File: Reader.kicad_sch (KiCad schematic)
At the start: 41 parts, among them J1 Conn_01x04, J2 Amphenol Dubox ‎76383-402LF‎, J3 Conn_01x04, J4 Conn_01x08, J5 Conn_01x10, J6 Conn_01x03, J7 Conn_01x02, Q1 2N7002, Q2 2N7002, Q3 2N7002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

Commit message: Enlarge mounting holes
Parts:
- H1, H2, H3: footprint MountingHole:MountingHole_2.5mm -> MountingHole:MountingHole_3.2mm_M3
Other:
- note added: "TODO: - Mark LED + on silk - Cut groundplane below cutout to prevent making loop/antenna. - Resistor values on silk? - 2N7002 hand soldering footprint - Reduce thermal size (esp C1 and transistors). Maybe just remove traces, or also -0,05mm? - decoupling/buffer caps? - Use only 1 GND of NFC reader(for EMI)? - Remove 45deg silkscreen line at J1 Done: - Removed optional from pulldowns, made value 1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"
- note removed: "TODO: - Mark LED + on silk - Cut groundplane below cutout to prevent making loop/antenna. - Resistor values on silk? - 2N7002 hand soldering footprint - Reduce thermal size (esp C1 and transistors). Maybe just remove traces, or also -0,05mm? - decoupling/buffer caps? - Use only 1 GND of NFC reader(for EMI)? - Remove 45deg silkscreen line at J1 - Larger holes 3.2mm Done: - Removed optional from pu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"
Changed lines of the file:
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@@
     (stroke (width 0) (type default))
   )
-  (text "TODO:\n - Mark LED + on silk\n - Cut groundplane below cutout to prevent making loop/antenna.\n - Resistor values on silk?\n - 2N7002 hand soldering footprint\n - Reduce thermal size (esp C1 and transistors). Maybe just remove traces, or also -0,05mm?\n - decoupling/buffer caps?\n - Use only 1 GND of NFC reader(for EMI)?\n - Remove 45deg silkscreen line at J1\n - Larger holes 3.2mm\n\nDone:\n - Removed optional from pulldowns, made value 1k.\n - Added series resistors for button input\n - Added C2 to suppress output pin pulses"
+  (text "TODO:\n - Mark LED + on silk\n - Cut groundplane below cutout to prevent making loop/antenna.\n - Resistor values on silk?\n - 2N7002 hand soldering footprint\n - Reduce thermal size (esp C1 and transistors). Maybe just remove traces, or also -0,05mm?\n - decoupling/buffer caps?\n - Use only 1 GND of NFC reader(for EMI)?\n - Remove 45deg silkscreen line at J1\n\nDone:\n - Removed optional from pulldowns, made value 1k.\n - Added series resistors for button input\n - Added C2 to suppress output pin pulses\n - Enlarged mounting holes from 2.5mm to 3.2mm\n"
     (at 116.84 152.4 0)
     (effects (font (size 1.27 1.27)) (justify left bottom))
@@
       (effects (font (size 1.27 1.27)) (justify left))
     )
-    (property "Footprint" "MountingHole:MountingHole_2.5mm" (at 265.43 147.32 0)
+    (property "Footprint" "MountingHole:MountingHole_3.2mm_M3" (at 265.43 147.32 0)
       (effects (font (size 1.27 1.27)) hide)
     )
@@
       (effects (font (size 1.27 1.27)) (justify left))
     )
-    (property "Footprint" "MountingHole:MountingHole_2.5mm" (at 265.43 153.67 0)
+    (property "Footprint" "MountingHole:MountingHole_3.2mm_M3" (at 265.43 153.67 0)
       (effects (font (size 1.27 1.27)) hide)
     )
@@
       (effects (font (size 1.27 1.27)) (justify left))
     )
-    (property "Footprint" "MountingHole:MountingHole_2.5mm" (at 265.43 160.02 0)
-      (effects (font (size 1.27 1.27)) hide)
-    )
+    (property "Footprint" "MountingHole:MountingHole_3.2mm_M3" (at 265.43 160.02 0)
+      (effects (font (size 1.27 1.27)) hide)
+    )

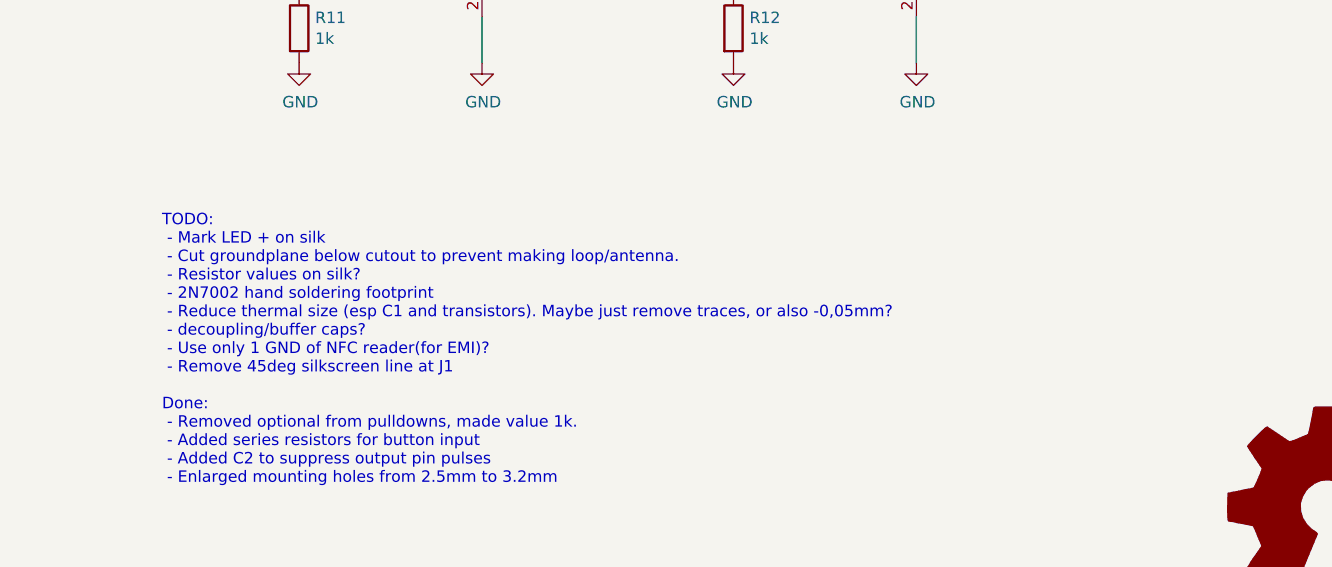
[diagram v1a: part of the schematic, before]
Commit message: Remove groundloop-related todos
It seems that having multiple GND connections and a hole inside the GND
plane might not actually be problematic (or if it is, making a horseshoe
out of it might not make it better).

So for now, leave this as is until it is actually a problem.
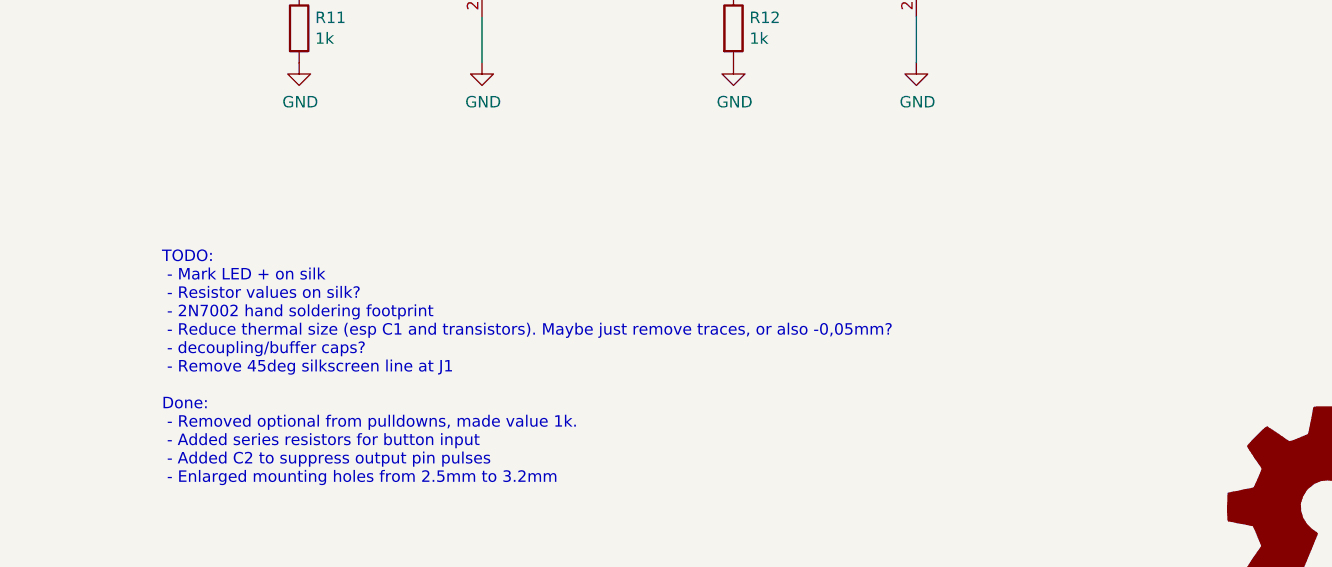
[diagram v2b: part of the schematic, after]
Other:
- note added: "TODO: - Mark LED + on silk - Resistor values on silk? - 2N7002 hand soldering footprint - Reduce thermal size (esp C1 and transistors). Maybe just remove traces, or also -0,05mm? - decoupling/buffer caps? - Remove 45deg silkscreen line at J1 Done: - Removed optional from pulldowns, made value 1k. - Added series resistors for button input - Added C2 to suppress output pin pulses - Enlarged mountin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"
- note removed: "TODO: - Mark LED + on silk - Cut groundplane below cutout to prevent making loop/antenna. - Resistor values on silk? - 2N7002 hand soldering footprint - Reduce thermal size (esp C1 and transistors). Maybe just remove traces, or also -0,05mm? - decoupling/buffer caps? - Use only 1 GND of NFC reader(for EMI)? - Remove 45deg silkscreen line at J1 Done: - Removed optional from pulldowns, made value 1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"
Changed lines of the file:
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@@
     (stroke (width 0) (type default))
   )
-  (text "TODO:\n - Mark LED + on silk\n - Cut groundplane below cutout to prevent making loop/antenna.\n - Resistor values on silk?\n - 2N7002 hand soldering footprint\n - Reduce thermal size (esp C1 and transistors). Maybe just remove traces, or also -0,05mm?\n - decoupling/buffer caps?\n - Use only 1 GND of NFC reader(for EMI)?\n - Remove 45deg silkscreen line at J1\n\nDone:\n - Removed optional from pulldowns, made value 1k.\n - Added series resistors for button input\n - Added C2 to suppress output pin pulses\n - Enlarged mounting holes from 2.5mm to 3.2mm\n"
+  (text "TODO:\n - Mark LED + on silk\n - Resistor values on silk?\n - 2N7002 hand soldering footprint\n - Reduce thermal size (esp C1 and transistors). Maybe just remove traces, or also -0,05mm?\n - decoupling/buffer caps?\n - Remove 45deg silkscreen line at J1\n\nDone:\n - Removed optional from pulldowns, made value 1k.\n - Added series resistors for button input\n - Added C2 to suppress output pin pulses\n - Enlarged mounting holes from 2.5mm to 3.2mm\n"
     (at 116.84 152.4 0)
     (effects (font (size 1.27 1.27)) (justify left bottom))

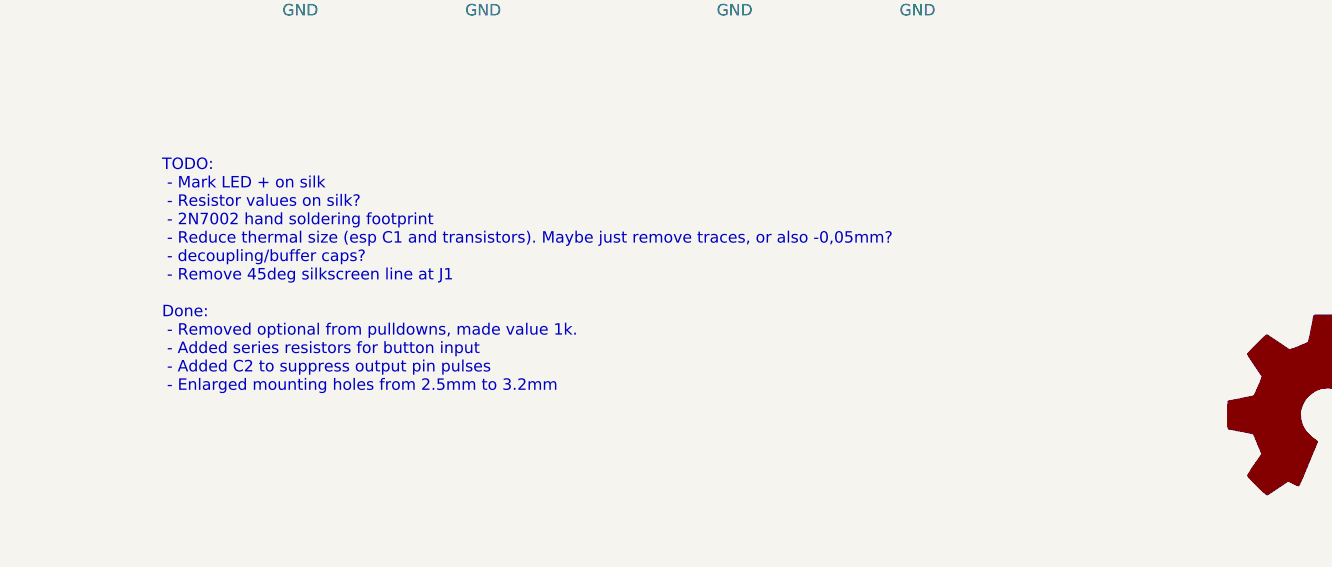
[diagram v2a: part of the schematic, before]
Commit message: Mark LED polarity on silkscreen
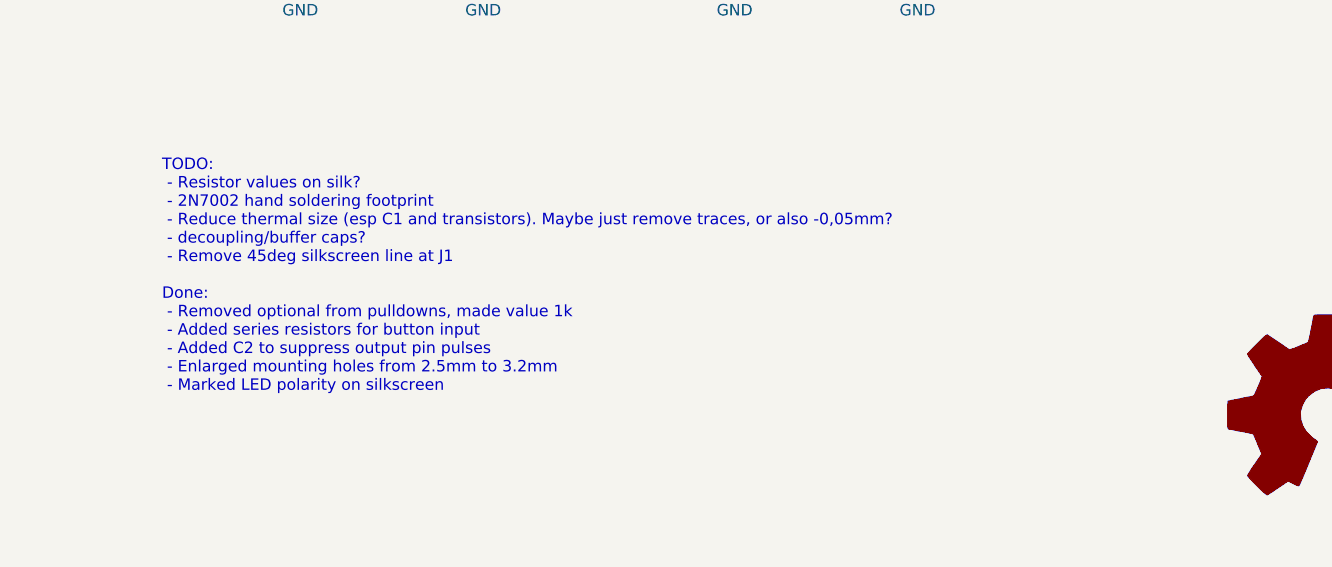
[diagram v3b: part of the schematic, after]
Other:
- note added: "TODO: - Resistor values on silk? - 2N7002 hand soldering footprint - Reduce thermal size (esp C1 and transistors). Maybe just remove traces, or also -0,05mm? - decoupling/buffer caps? - Remove 45deg silkscreen line at J1 Done: - Removed optional from pulldowns, made value 1k - Added series resistors for button input - Added C2 to suppress output pin pulses - Enlarged mounting holes from 2.5mm to 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"
- note removed: "TODO: - Mark LED + on silk - Resistor values on silk? - 2N7002 hand soldering footprint - Reduce thermal size (esp C1 and transistors). Maybe just remove traces, or also -0,05mm? - decoupling/buffer caps? - Remove 45deg silkscreen line at J1 Done: - Removed optional from pulldowns, made value 1k. - Added series resistors for button input - Added C2 to suppress output pin pulses - Enlarged mountin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"
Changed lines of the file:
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@@
     (stroke (width 0) (type default))
   )
-  (text "TODO:\n - Mark LED + on silk\n - Resistor values on silk?\n - 2N7002 hand soldering footprint\n - Reduce thermal size (esp C1 and transistors). Maybe just remove traces, or also -0,05mm?\n - decoupling/buffer caps?\n - Remove 45deg silkscreen line at J1\n\nDone:\n - Removed optional from pulldowns, made value 1k.\n - Added series resistors for button input\n - Added C2 to suppress output pin pulses\n - Enlarged mounting holes from 2.5mm to 3.2mm\n"
+  (text "TODO:\n - Resistor values on silk?\n - 2N7002 hand soldering footprint\n - Reduce thermal size (esp C1 and transistors). Maybe just remove traces, or also -0,05mm?\n - decoupling/buffer caps?\n - Remove 45deg silkscreen line at J1\n\nDone:\n - Removed optional from pulldowns, made value 1k\n - Added series resistors for button input\n - Added C2 to suppress output pin pulses\n - Enlarged mounting holes from 2.5mm to 3.2mm\n - Marked LED polarity on silkscreen\n"
     (at 116.84 152.4 0)
     (effects (font (size 1.27 1.27)) (justify left bottom))

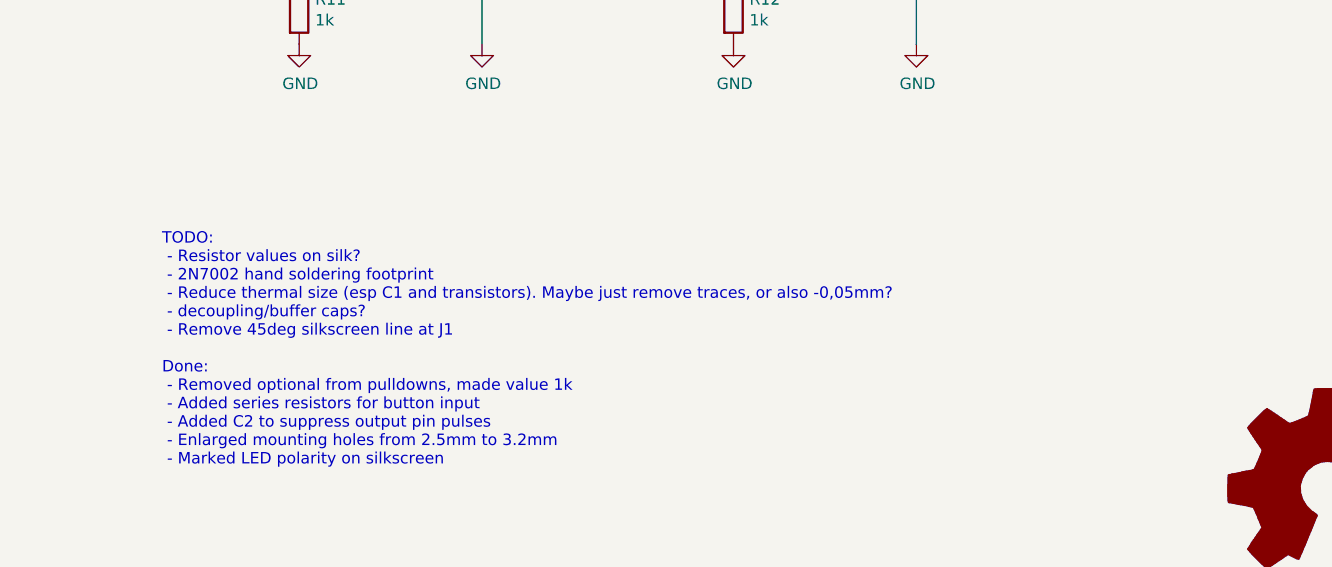
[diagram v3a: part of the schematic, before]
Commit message: Remove unintended silkscreen line
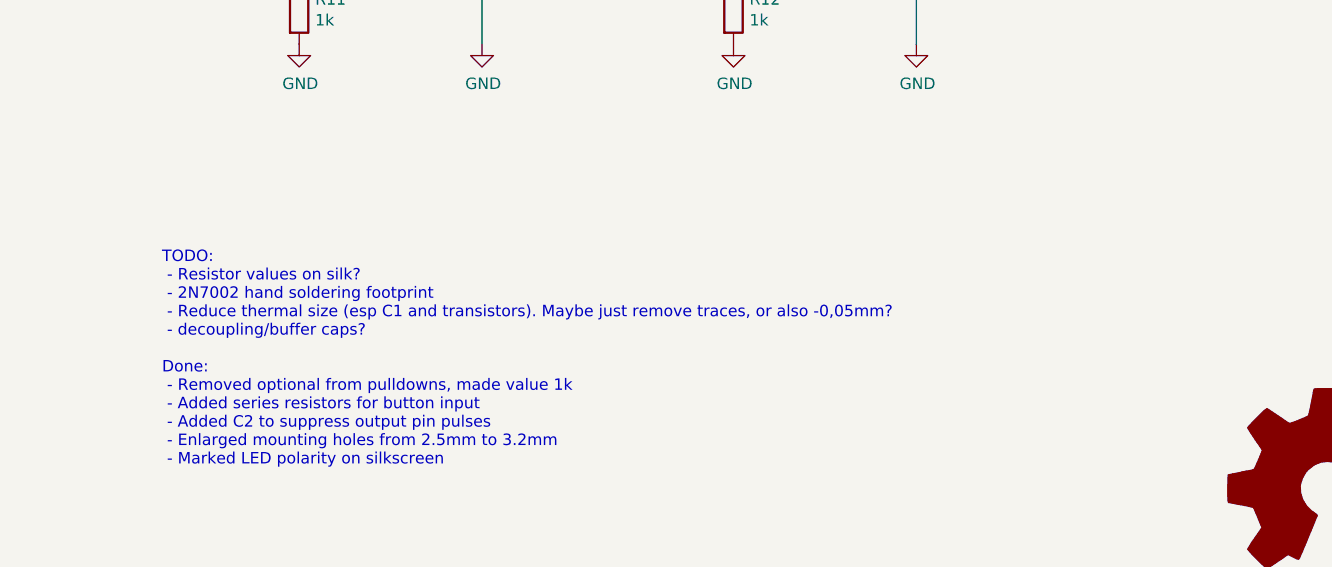
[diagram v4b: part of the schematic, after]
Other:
- note added: "TODO: - Resistor values on silk? - 2N7002 hand soldering footprint - Reduce thermal size (esp C1 and transistors). Maybe just remove traces, or also -0,05mm? - decoupling/buffer caps? Done: - Removed optional from pulldowns, made value 1k - Added series resistors for button input - Added C2 to suppress output pin pulses - Enlarged mounting holes from 2.5mm to 3.2mm - Marked LED polarity on silksc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"
- note removed: "TODO: - Resistor values on silk? - 2N7002 hand soldering footprint - Reduce thermal size (esp C1 and transistors). Maybe just remove traces, or also -0,05mm? - decoupling/buffer caps? - Remove 45deg silkscreen line at J1 Done: - Removed optional from pulldowns, made value 1k - Added series resistors for button input - Added C2 to suppress output pin pulses - Enlarged mounting holes from 2.5mm to 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"
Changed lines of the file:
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@@
     (stroke (width 0) (type default))
   )
-  (text "TODO:\n - Resistor values on silk?\n - 2N7002 hand soldering footprint\n - Reduce thermal size (esp C1 and transistors). Maybe just remove traces, or also -0,05mm?\n - decoupling/buffer caps?\n - Remove 45deg silkscreen line at J1\n\nDone:\n - Removed optional from pulldowns, made value 1k\n - Added series resistors for button input\n - Added C2 to suppress output pin pulses\n - Enlarged mounting holes from 2.5mm to 3.2mm\n - Marked LED polarity on silkscreen\n"
+  (text "TODO:\n - Resistor values on silk?\n - 2N7002 hand soldering footprint\n - Reduce thermal size (esp C1 and transistors). Maybe just remove traces, or also -0,05mm?\n - decoupling/buffer caps?\n\nDone:\n - Removed optional from pulldowns, made value 1k\n - Added series resistors for button input\n - Added C2 to suppress output pin pulses\n - Enlarged mounting holes from 2.5mm to 3.2mm\n - Marked LED polarity on silkscreen\n"
     (at 116.84 152.4 0)
     (effects (font (size 1.27 1.27)) (justify left bottom))
